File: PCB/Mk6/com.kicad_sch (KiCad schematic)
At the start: 5 parts, among them J9 COM: Gnd,CTS, Vcc, Tx, Rx, DTR, U7 MC68B50

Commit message: save
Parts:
- renumbered JP27 to JP5, JP1 to JP6, R25 to R4, U7 to U9
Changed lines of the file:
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@@
 		(on_board yes)
 		(dnp no)
-		(property "Reference" "R25"
+		(property "Reference" "R4"
 			(at 36.83 57.658 90)
 			(effects
@@
 			(project "Mk6"
 				(path "/d41350ce-2040-418d-ae11-f076a5474776/87fe3d26-27b8-42b5-bb91-53d69d084d06"
-					(reference "R25")
+					(reference "R4")
 					(unit 1)
 				)
@@
 		(dnp no)
 		(fields_autoplaced yes)
-		(property "Reference" "JP27"
+		(property "Reference" "JP5"
 			(at 26.67 59.69 0)
 			(effects
@@
 			(project "Mk6"
 				(path "/d41350ce-2040-418d-ae11-f076a5474776/87fe3d26-27b8-42b5-bb91-53d69d084d06"
-					(reference "JP27")
+					(reference "JP5")
 					(unit 1)
 				)
@@
 		(dnp no)
 		(fields_autoplaced yes)
-		(property "Reference" "#PWR029"
+		(property "Reference" "#PWR033"
 			(at 41.91 86.36 0)
 			(effects
@@
 			(project "Mk6"
 				(path "/d41350ce-2040-418d-ae11-f076a5474776/87fe3d26-27b8-42b5-bb91-53d69d084d06"
-					(reference "#PWR029")
+					(reference "#PWR033")
 					(unit 1)
 				)
@@
 		(on_board yes)
 		(dnp no)
-		(property "Reference" "#PWR019"
+		(property "Reference" "#PWR029"
 			(at 93.98 66.04 0)
 			(effects
@@
 			(project "Mk6"
 				(path "/d41350ce-2040-418d-ae11-f076a5474776/87fe3d26-27b8-42b5-bb91-53d69d084d06"
-					(reference "#PWR019")
+					(reference "#PWR029")
 					(unit 1)
 				)
@@
 		(on_board yes)
 		(dnp no)
-		(property "Reference" "JP1"
+		(property "Reference" "JP6"
 			(at 87.122 78.994 90)
 			(effects
@@
 			(project "Mk6"
 				(path "/d41350ce-2040-418d-ae11-f076a5474776/87fe3d26-27b8-42b5-bb91-53d69d084d06"
-					(reference "JP1")
+					(reference "JP6")
 					(unit 1)
 				)
@@
 		(on_board yes)
 		(dnp no)
-		(property "Reference" "#PWR032"
+		(property "Reference" "#PWR026"
 			(at 25.4 49.53 0)
 			(effects
@@
 			(project "Mk6"
 				(path "/d41350ce-2040-418d-ae11-f076a5474776/87fe3d26-27b8-42b5-bb91-53d69d084d06"
-					(reference "#PWR032")
+					(reference "#PWR026")
 					(unit 1)
 				)
@@
 		(dnp no)
 		(fields_autoplaced yes)
-		(property "Reference" "#PWR018"
+		(property "Reference" "#PWR022"
 			(at 92.71 25.4 0)
 			(effects
@@
 			(project "Mk6"
 				(path "/d41350ce-2040-418d-ae11-f076a5474776/87fe3d26-27b8-42b5-bb91-53d69d084d06"
-					(reference "#PWR018")
+					(reference "#PWR022")
 					(unit 1)
 				)
@@
 		(on_board yes)
 		(dnp no)
-		(property "Reference" "U7"
+		(property "Reference" "U9"
 			(at 88.138 37.084 0)
 			(effects
@@
 			(project "Mk6"
 				(path "/d41350ce-2040-418d-ae11-f076a5474776/87fe3d26-27b8-42b5-bb91-53d69d084d06"
-					(reference "U7")
+					(reference "U9")
 					(unit 1)
 				)
@@
 		(dnp no)
 		(fields_autoplaced yes)
-		(property "Reference" "#PWR034"
+		(property "Reference" "#PWR031"
 			(at 19.05 72.39 0)
 			(effects
@@
 			(project "Mk6"
 				(path "/d41350ce-2040-418d-ae11-f076a5474776/87fe3d26-27b8-42b5-bb91-53d69d084d06"
-					(reference "#PWR034")
-					(unit 1)
-				)
+					(reference "#PWR031")
+					(unit 1)
+				)

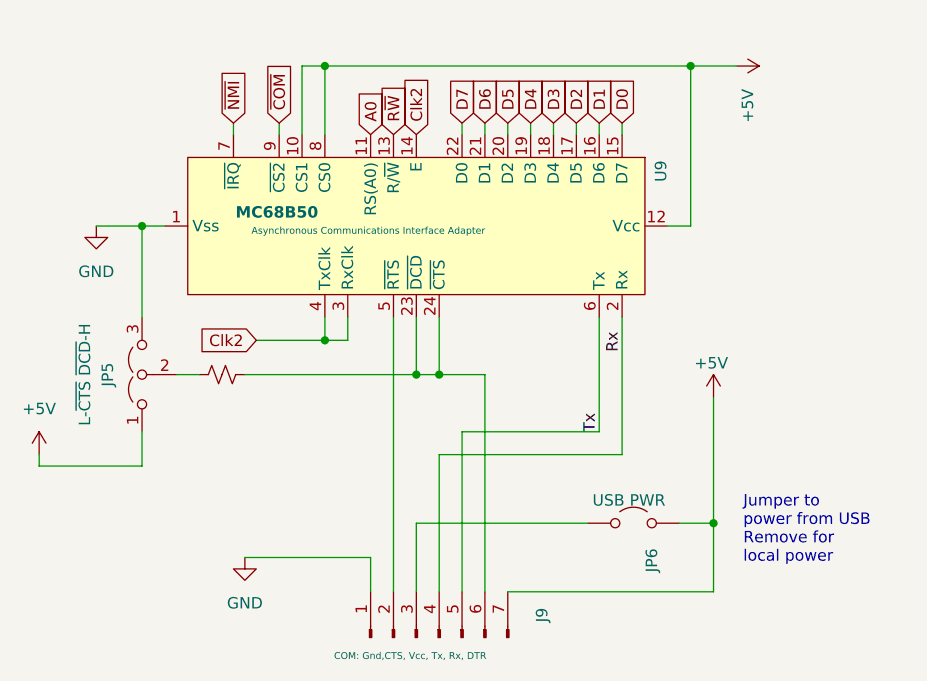
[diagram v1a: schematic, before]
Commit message: all done, pre-clk div
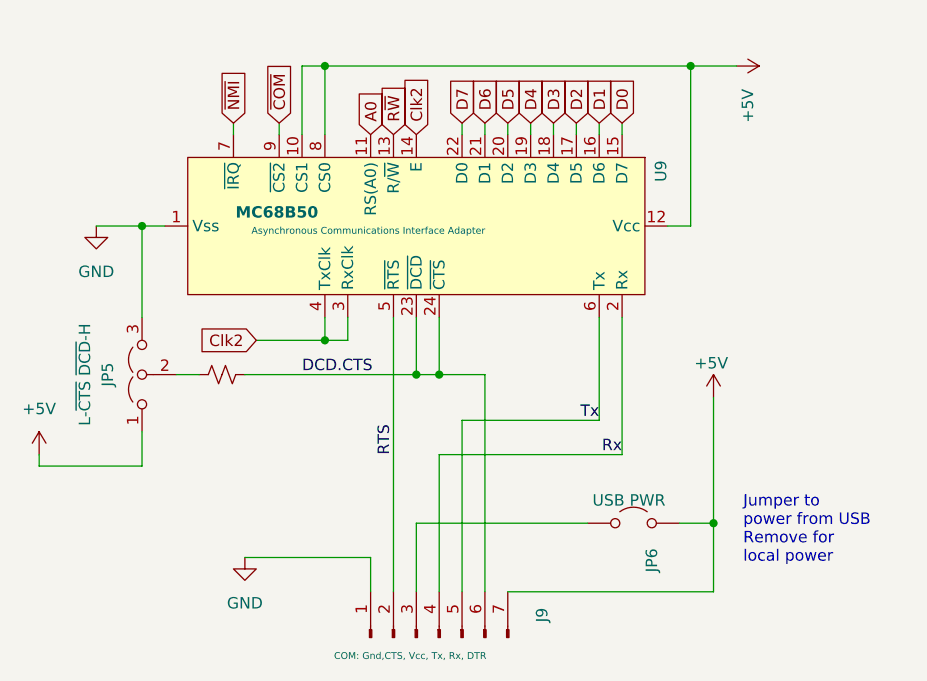
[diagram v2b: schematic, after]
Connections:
- net RTS: now reaches J9.2 (Pin_2), U9.5 (~{RTS})
- net DCD.CTS: now reaches J9.6 (Pin_6), R4.2, U9.23 (~{DCD}), U9.24 (~{CTS})
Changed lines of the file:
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@@
 	(wire
 		(pts
-			(xy 81.28 53.34) (xy 81.28 66.04)
+			(xy 81.28 53.34) (xy 81.28 64.77)
 		)
 		(stroke
@@
 	(wire
 		(pts
-			(xy 66.04 66.04) (xy 66.04 83.82)
+			(xy 66.04 64.77) (xy 66.04 83.82)
 		)
 		(stroke
@@
 	(wire
 		(pts
-			(xy 81.28 66.04) (xy 66.04 66.04)
+			(xy 81.28 64.77) (xy 66.04 64.77)
 		)
 		(stroke
@@
 		)
 	)
+	(label "RTS"
+		(at 58.42 68.58 90)
+		(effects
+			(font
+				(size 1.27 1.27)
+			)
+			(justify left bottom)
+		)
+	)
 	(label "Tx"
-		(at 81.28 66.04 90)
+		(at 81.28 64.77 180)
+		(effects
+			(font
+				(size 1.27 1.27)
+			)
+			(justify right bottom)
+		)
+	)
+	(label "DCD.CTS"
+		(at 48.26 59.69 0)
 		(effects
 			(font
@@
 	)
 	(label "Rx"
-		(at 83.82 57.15 90)
-		(effects
-			(font
-				(size 1.27 1.27)
-			)
-			(justify left bottom)
-		)
-	)
+		(at 83.82 68.58 180)
+		(effects
+			(font
+				(size 1.27 1.27)
+			)
+			(justify right bottom)
+		)
+	)

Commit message: Cleaned
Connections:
- net Clk2: no longer U9.3 (RxClk), U9.4 (TxClk)
- new net BaudClk: U9.3 (RxClk), U9.4 (TxClk)
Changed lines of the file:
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@@
 		)
 	)
-	(global_label "Clk2"
+	(global_label "BaudClk"
 		(shape input)
 		(at 43.18 55.88 180)
@@
 		)
 		(property "Intersheetrefs" "${INTERSHEET_REFS}"
-			(at 36.022 55.88 0)
+			(at 32.5145 55.88 0)
 			(effects
 				(font

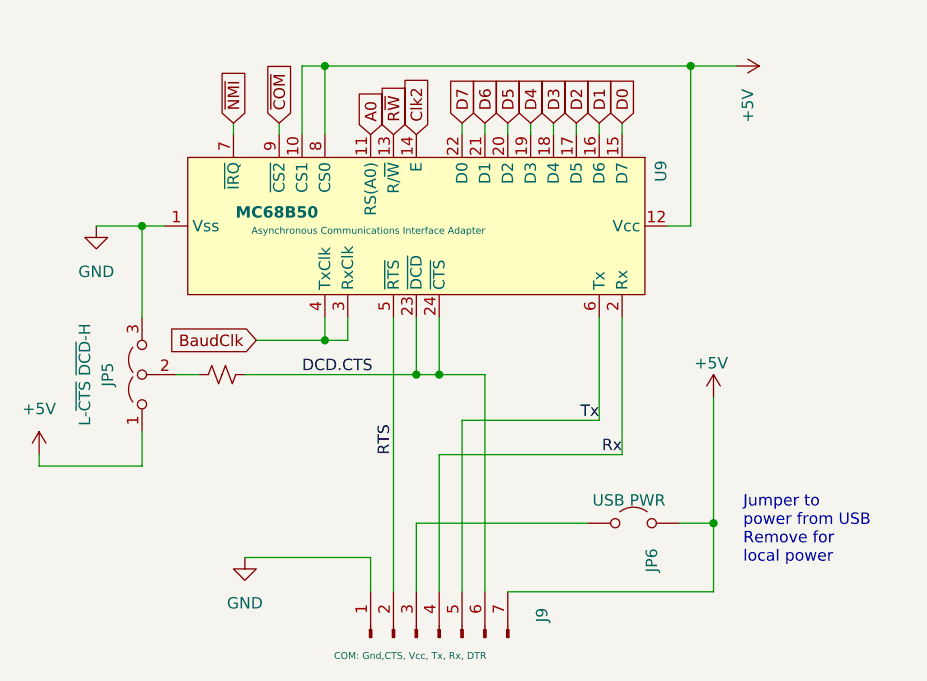
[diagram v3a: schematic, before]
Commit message: Added 3-8 IO, extra GAL out, attachment point for !RAM
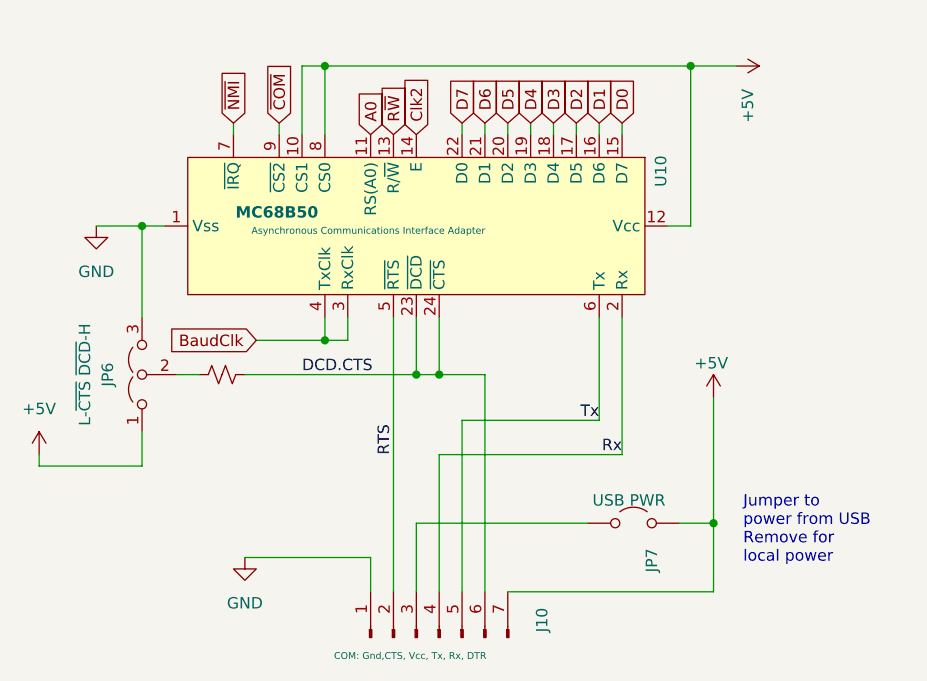
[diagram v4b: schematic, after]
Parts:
- renumbered J9 to J10, JP5 to JP6, JP6 to JP7, U9 to U10
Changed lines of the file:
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@@
 		(on_board yes)
 		(dnp no)
-		(property "Reference" "J9"
+		(property "Reference" "J10"
 			(at 74.93 85.598 0)
 			(effects
@@
 			(project "Mk6"
 				(path "/d41350ce-2040-418d-ae11-f076a5474776/87fe3d26-27b8-42b5-bb91-53d69d084d06"
-					(reference "J9")
+					(reference "J10")
 					(unit 1)
 				)
@@
 		(dnp no)
 		(fields_autoplaced yes)
-		(property "Reference" "JP5"
+		(property "Reference" "JP6"
 			(at 26.67 59.69 0)
 			(effects
@@
 			(project "Mk6"
 				(path "/d41350ce-2040-418d-ae11-f076a5474776/87fe3d26-27b8-42b5-bb91-53d69d084d06"
-					(reference "JP5")
+					(reference "JP6")
 					(unit 1)
 				)
@@
 		(dnp no)
 		(fields_autoplaced yes)
-		(property "Reference" "#PWR033"
+		(property "Reference" "#PWR034"
 			(at 41.91 86.36 0)
 			(effects
@@
 			(project "Mk6"
 				(path "/d41350ce-2040-418d-ae11-f076a5474776/87fe3d26-27b8-42b5-bb91-53d69d084d06"
-					(reference "#PWR033")
+					(reference "#PWR034")
 					(unit 1)
 				)
@@
 		(on_board yes)
 		(dnp no)
-		(property "Reference" "#PWR029"
+		(property "Reference" "#PWR030"
 			(at 93.98 66.04 0)
 			(effects
@@
 			(project "Mk6"
 				(path "/d41350ce-2040-418d-ae11-f076a5474776/87fe3d26-27b8-42b5-bb91-53d69d084d06"
-					(reference "#PWR029")
+					(reference "#PWR030")
 					(unit 1)
 				)
@@
 		(on_board yes)
 		(dnp no)
-		(property "Reference" "JP6"
+		(property "Reference" "JP7"
 			(at 87.122 78.994 90)
 			(effects
@@
 			(project "Mk6"
 				(path "/d41350ce-2040-418d-ae11-f076a5474776/87fe3d26-27b8-42b5-bb91-53d69d084d06"
-					(reference "JP6")
+					(reference "JP7")
 					(unit 1)
 				)
@@
 		(on_board yes)
 		(dnp no)
-		(property "Reference" "#PWR026"
+		(property "Reference" "#PWR027"
 			(at 25.4 49.53 0)
 			(effects
@@
 			(project "Mk6"
 				(path "/d41350ce-2040-418d-ae11-f076a5474776/87fe3d26-27b8-42b5-bb91-53d69d084d06"
-					(reference "#PWR026")
+					(reference "#PWR027")
 					(unit 1)
 				)
@@
 		(dnp no)
 		(fields_autoplaced yes)
-		(property "Reference" "#PWR022"
+		(property "Reference" "#PWR023"
 			(at 92.71 25.4 0)
 			(effects
@@
 			(project "Mk6"
 				(path "/d41350ce-2040-418d-ae11-f076a5474776/87fe3d26-27b8-42b5-bb91-53d69d084d06"
-					(reference "#PWR022")
+					(reference "#PWR023")
 					(unit 1)
 				)
@@
 		(on_board yes)
 		(dnp no)
-		(property "Reference" "U9"
+		(property "Reference" "U10"
 			(at 88.138 37.084 0)
 			(effects
@@
 			(project "Mk6"
 				(path "/d41350ce-2040-418d-ae11-f076a5474776/87fe3d26-27b8-42b5-bb91-53d69d084d06"
-					(reference "U9")
+					(reference "U10")
 					(unit 1)
 				)
@@
 		(dnp no)
 		(fields_autoplaced yes)
-		(property "Reference" "#PWR031"
+		(property "Reference" "#PWR032"
 			(at 19.05 72.39 0)
 			(effects
@@
 			(project "Mk6"
 				(path "/d41350ce-2040-418d-ae11-f076a5474776/87fe3d26-27b8-42b5-bb91-53d69d084d06"
-					(reference "#PWR031")
-					(unit 1)
-				)
+					(reference "#PWR032")
+					(unit 1)
+				)

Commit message: cleanup
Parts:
- J10: value COM: Gnd,CTS, Vcc, Tx, Rx, DTR -> COM: Gnd, RTS, Vcc, Rx, Tx, DCD-CTS, 5v
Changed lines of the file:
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@@
 			)
 		)
-		(property "Value" "COM: Gnd,CTS, Vcc, Tx, Rx, DTR"
+		(property "Value" "COM: Gnd, RTS, Vcc, Rx, Tx, DCD-CTS, 5v"
 			(at 51.816 90.932 90)
 			(effects
